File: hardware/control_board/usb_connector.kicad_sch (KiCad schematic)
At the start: 6 parts, among them J5 USB_C, U4 USBLC6-2SC6

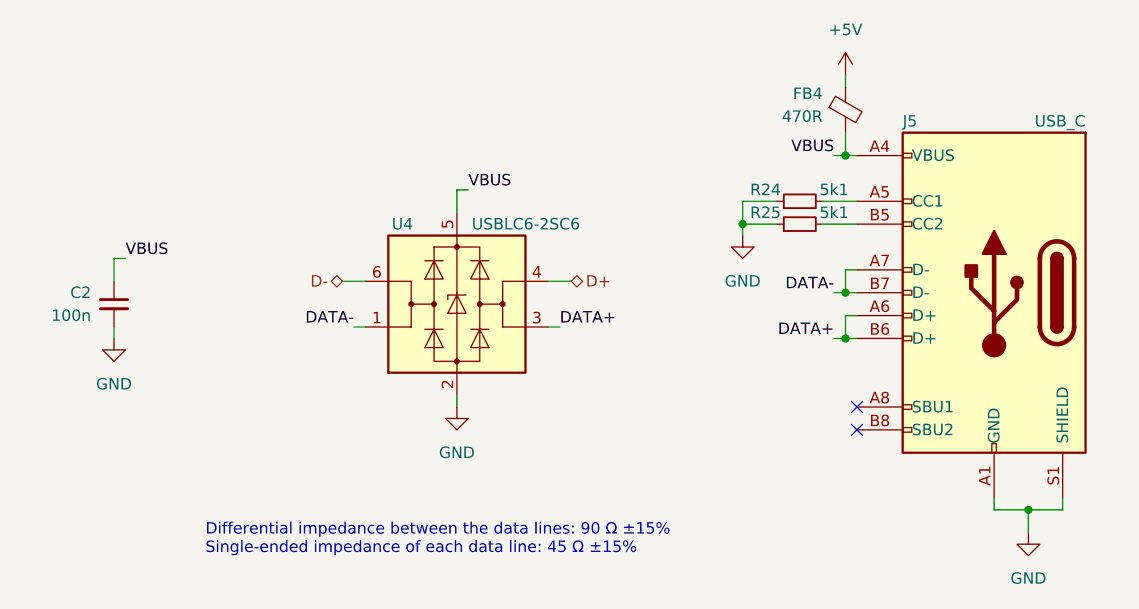
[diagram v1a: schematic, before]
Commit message: Change the buzzer
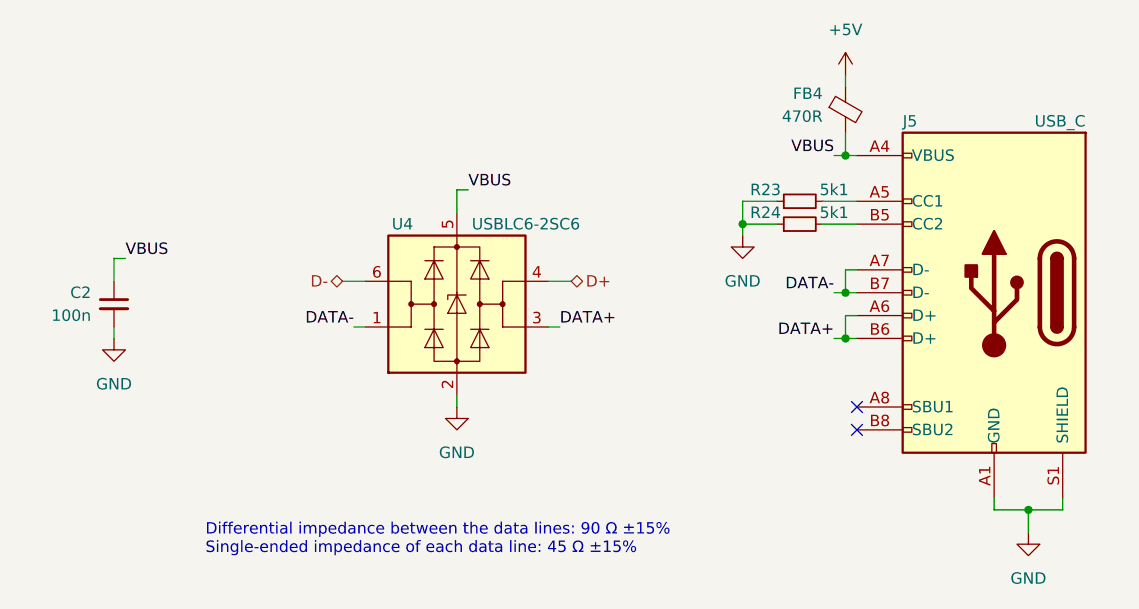
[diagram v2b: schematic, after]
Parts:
- J5: footprint Connector_USB:USB_C_Receptacle_GCT_USB4105-xx-A_16P_TopMnt_Horizontal -> Local_Library:USB4105-GF-A
- renumbered R24 to R23, R25 to R24
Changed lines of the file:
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@@
   (symbol (lib_id "Device:R_Small") (at 175.26 91.44 90) (unit 1)
     (in_bom yes) (on_board yes) (dnp no)
-    (property "Reference" "R25" (at 171.45 90.17 90)
+    (property "Reference" "R24" (at 171.45 90.17 90)
       (effects (font (size 1.27 1.27)))
     )
@@
       (project "control_board"
         (path "/b652b05a-4e3d-4ad1-b032-18886abe7d45/3d0d4351-20fe-44b0-a348-a3114badfe96"
-          (reference "R25") (unit 1)
+          (reference "R24") (unit 1)
         )
       )
@@
   (symbol (lib_id "Device:R_Small") (at 175.26 88.9 90) (unit 1)
     (in_bom yes) (on_board yes) (dnp no)
-    (property "Reference" "R24" (at 171.45 87.63 90)
+    (property "Reference" "R23" (at 171.45 87.63 90)
       (effects (font (size 1.27 1.27)))
     )
@@
       (project "control_board"
         (path "/b652b05a-4e3d-4ad1-b032-18886abe7d45/3d0d4351-20fe-44b0-a348-a3114badfe96"
-          (reference "R24") (unit 1)
+          (reference "R23") (unit 1)
         )
       )
@@
       (effects (font (size 1.27 1.27)) (justify left))
     )
-    (property "Footprint" "Connector_USB:USB_C_Receptacle_GCT_USB4105-xx-A_16P_TopMnt_Horizontal" (at 193.04 99.06 0)
+    (property "Footprint" "Local_Library:USB4105-GF-A" (at 193.04 99.06 0)
       (effects (font (size 1.27 1.27)) hide)
     )

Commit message: Add USB D+ pull-up resistor
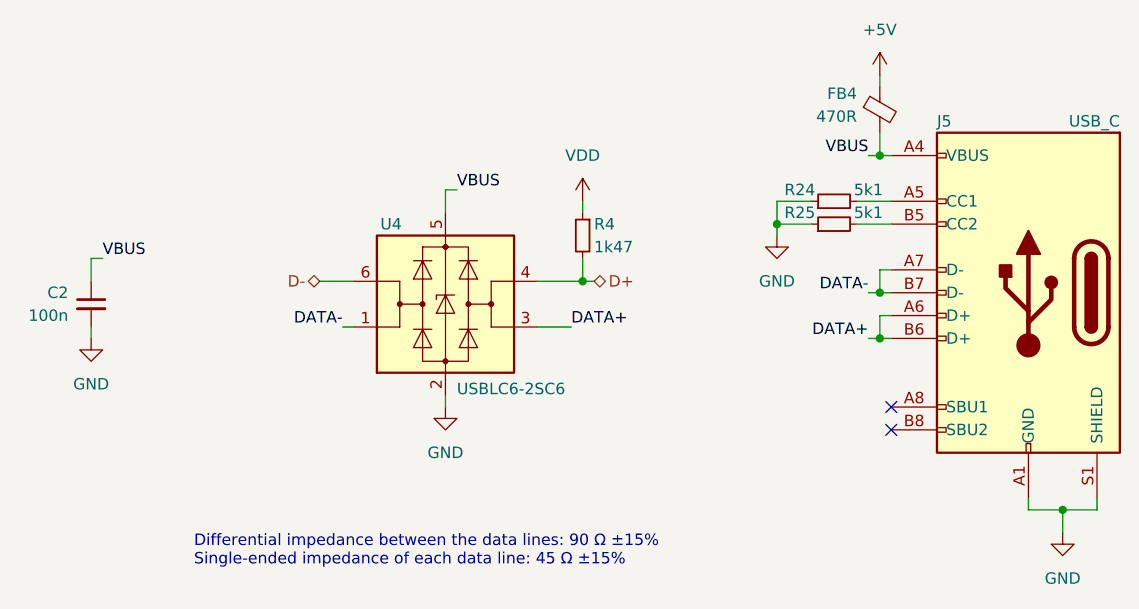
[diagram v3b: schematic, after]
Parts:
- added R4: 1k47, Resistor_SMD:R_0603_1608Metric, symbol Device:R_Small
- renumbered R23 to R24, R24 to R25
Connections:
- net D+: now also R4.2
- new net VDD: R4.1
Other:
- moved on the sheet: C2, FB4, J5, R24, R25, U4

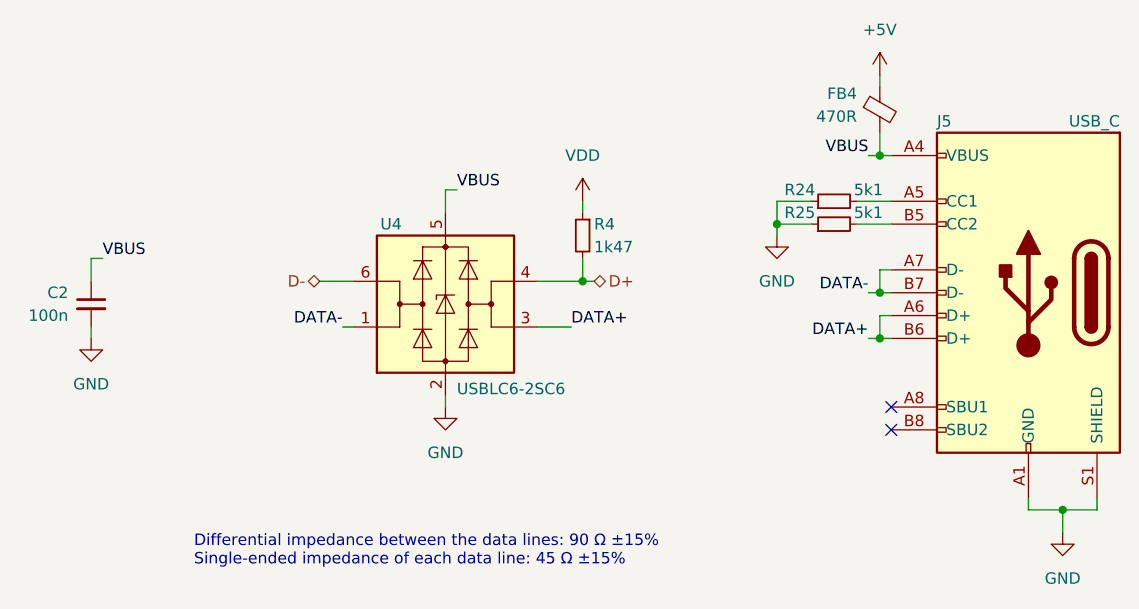
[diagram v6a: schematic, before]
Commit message: Update reference designators
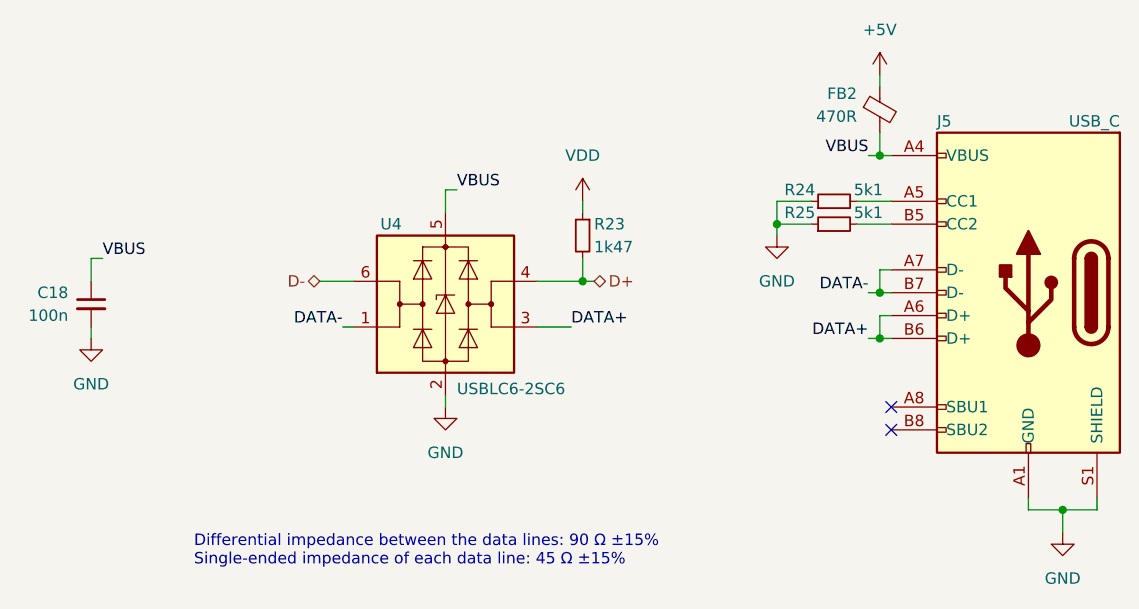
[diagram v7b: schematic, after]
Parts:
- J5: symbol Connector:USB_C_Receptacle_USB2.0 -> Connector:USB_C_Receptacle_USB2.0_16P
- renumbered C2 to C18, FB4 to FB2, R4 to R23
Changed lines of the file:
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@@
   (symbol (lib_id "power:GND") (at 172.72 92.71 0) (mirror y) (unit 1)
     (in_bom yes) (on_board yes) (dnp no)
-    (property "Reference" "#PWR?" (at 172.72 99.06 0)
+    (property "Reference" "#PWR059" (at 172.72 99.06 0)
       (effects (font (size 1.27 1.27)) hide)
     )
@@
     (instances
       (project "control_board"
-        (path "/b652b05a-4e3d-4ad1-b032-18886abe7d45"
-          (reference "#PWR?") (unit 1)
-        )
-        (path "/b652b05a-4e3d-4ad1-b032-18886abe7d45/02711725-e382-48ba-bf33-23fe46c66e66"
-          (reference "#PWR023") (unit 1)
-        )
         (path "/b652b05a-4e3d-4ad1-b032-18886abe7d45/3d0d4351-20fe-44b0-a348-a3114badfe96"
           (reference "#PWR059") (unit 1)
@@
   (symbol (lib_id "power:GND") (at 204.47 125.73 0) (mirror y) (unit 1)
     (in_bom yes) (on_board yes) (dnp no)
-    (property "Reference" "#PWR?" (at 204.47 132.08 0)
+    (property "Reference" "#PWR061" (at 204.47 132.08 0)
       (effects (font (size 1.27 1.27)) hide)
     )
@@
     (instances
       (project "control_board"
-        (path "/b652b05a-4e3d-4ad1-b032-18886abe7d45"
-          (reference "#PWR?") (unit 1)
-        )
-        (path "/b652b05a-4e3d-4ad1-b032-18886abe7d45/02711725-e382-48ba-bf33-23fe46c66e66"
-          (reference "#PWR023") (unit 1)
-        )
         (path "/b652b05a-4e3d-4ad1-b032-18886abe7d45/3d0d4351-20fe-44b0-a348-a3114badfe96"
           (reference "#PWR061") (unit 1)
@@
   (symbol (lib_id "Device:R_Small") (at 151.13 92.71 0) (mirror y) (unit 1)
     (in_bom yes) (on_board yes) (dnp no)
-    (property "Reference" "R4" (at 152.4 91.44 0)
+    (property "Reference" "R23" (at 152.4 91.44 0)
       (effects (font (size 1.27 1.27)) (justify right))
     )
@@
     (instances
       (project "control_board"
-        (path "/b652b05a-4e3d-4ad1-b032-18886abe7d45"
-          (reference "R4") (unit 1)
-        )
         (path "/b652b05a-4e3d-4ad1-b032-18886abe7d45/3d0d4351-20fe-44b0-a348-a3114badfe96"
           (reference "R23") (unit 1)
@@
   (symbol (lib_id "power:+5V") (at 184.15 74.93 0) (mirror y) (unit 1)
     (in_bom yes) (on_board yes) (dnp no)
-    (property "Reference" "#PWR?" (at 184.15 78.74 0)
+    (property "Reference" "#PWR060" (at 184.15 78.74 0)
       (effects (font (size 1.27 1.27)) hide)
     )
@@
     (instances
       (project "control_board"
-        (path "/b652b05a-4e3d-4ad1-b032-18886abe7d45"
-          (reference "#PWR?") (unit 1)
-        )
-        (path "/b652b05a-4e3d-4ad1-b032-18886abe7d45/02711725-e382-48ba-bf33-23fe46c66e66"
-          (reference "#PWR022") (unit 1)
-        )
         (path "/b652b05a-4e3d-4ad1-b032-18886abe7d45/3d0d4351-20fe-44b0-a348-a3114badfe96"
           (reference "#PWR060") (unit 1)
@@
   (symbol (lib_id "power:GND") (at 96.52 104.14 0) (unit 1)
     (in_bom yes) (on_board yes) (dnp no)
-    (property "Reference" "#PWR?" (at 96.52 110.49 0)
+    (property "Reference" "#PWR056" (at 96.52 110.49 0)
       (effects (font (size 1.27 1.27)) hide)
     )
@@
     (instances
       (project "control_board"
-        (path "/b652b05a-4e3d-4ad1-b032-18886abe7d45"
-          (reference "#PWR?") (unit 1)
-        )
-        (path "/b652b05a-4e3d-4ad1-b032-18886abe7d45/02711725-e382-48ba-bf33-23fe46c66e66"
-          (reference "#PWR018") (unit 1)
-        )
         (path "/b652b05a-4e3d-4ad1-b032-18886abe7d45/3d0d4351-20fe-44b0-a348-a3114badfe96"
           (reference "#PWR056") (unit 1)
@@
   (symbol (lib_id "Device:C_Small") (at 96.52 100.33 0) (mirror y) (unit 1)
     (in_bom yes) (on_board yes) (dnp no)
-    (property "Reference" "C2" (at 93.98 99.06 0)
+    (property "Reference" "C18" (at 93.98 99.06 0)
       (effects (font (size 1.27 1.27)) (justify left))
     )
@@
     (instances
       (project "control_board"
-        (path "/b652b05a-4e3d-4ad1-b032-18886abe7d45/02711725-e382-48ba-bf33-23fe46c66e66"
-          (reference "C2") (unit 1)
-        )
         (path "/b652b05a-4e3d-4ad1-b032-18886abe7d45/3d0d4351-20fe-44b0-a348-a3114badfe96"
           (reference "C18") (unit 1)
@@
   (symbol (lib_id "power:VDD") (at 151.13 88.9 0) (unit 1)
     (in_bom yes) (on_board yes) (dnp no) (fields_autoplaced)
-    (property "Reference" "#PWR011" (at 151.13 92.71 0)
+    (property "Reference" "#PWR058" (at 151.13 92.71 0)
       (effects (font (size 1.27 1.27)) hide)
     )
@@
     (instances
       (project "control_board"
-        (path "/b652b05a-4e3d-4ad1-b032-18886abe7d45"
-          (reference "#PWR011") (unit 1)
-        )
         (path "/b652b05a-4e3d-4ad1-b032-18886abe7d45/3d0d4351-20fe-44b0-a348-a3114badfe96"
           (reference "#PWR058") (unit 1)
@@
   (symbol (lib_id "Device:FerriteBead_Small") (at 184.15 78.74 0) (unit 1)
     (in_bom yes) (on_board yes) (dnp no)
-    (property "Reference" "FB4" (at 181.61 76.2 0)
+    (property "Reference" "FB2" (at 181.61 76.2 0)
       (effects (font (size 1.27 1.27)) (justify right top))
     )
@@
     (instances
       (project "control_board"
-        (path "/b652b05a-4e3d-4ad1-b032-18886abe7d45/02711725-e382-48ba-bf33-23fe46c66e66"
-          (reference "FB4") (unit 1)
-        )
         (path "/b652b05a-4e3d-4ad1-b032-18886abe7d45/3d0d4351-20fe-44b0-a348-a3114badfe96"
           (reference "FB2") (unit 1)
@@
     )
   )
-  (symbol (lib_id "Connector:USB_C_Receptacle_USB2.0") (at 200.66 99.06 0) (mirror y) (unit 1)
+  (symbol (lib_id "Connector:USB_C_Receptacle_USB2.0_16P") (at 200.66 99.06 0) (mirror y) (unit 1)
     (in_bom yes) (on_board yes) (dnp no)
     (property "Reference" "J5" (at 190.5 80.01 0)
@@
       (effects (font (size 1.27 1.27)) hide)
     )
-    (property "Datasheet" "https://gct.co/files/drawings/usb4105.pdf" (at 196.85 99.06 0)
+    (property "Datasheet" "https://www.usb.org/sites/default/files/documents/usb_type-c.zip" (at 196.85 99.06 0)
       (effects (font (size 1.27 1.27)) hide)
     )
@@
   (symbol (lib_id "power:GND") (at 135.89 111.76 0) (unit 1)
     (in_bom yes) (on_board yes) (dnp no)
-    (property "Reference" "#PWR?" (at 135.89 118.11 0)
+    (property "Reference" "#PWR057" (at 135.89 118.11 0)
       (effects (font (size 1.27 1.27)) hide)
     )
@@
     (instances
       (project "control_board"
-        (path "/b652b05a-4e3d-4ad1-b032-18886abe7d45"
-          (reference "#PWR?") (unit 1)
-        )
-        (path "/b652b05a-4e3d-4ad1-b032-18886abe7d45/02711725-e382-48ba-bf33-23fe46c66e66"
-          (reference "#PWR021") (unit 1)
-        )
         (path "/b652b05a-4e3d-4ad1-b032-18886abe7d45/3d0d4351-20fe-44b0-a348-a3114badfe96"
           (reference "#PWR057") (unit 1)
